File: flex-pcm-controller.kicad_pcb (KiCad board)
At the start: 2 copper layers, 36.6 x 35.6 mm, 19 parts, among them K1 POWER, K2 LOAD, Q1 PNP, Q2 MOSFET_DGS, Q3 MOSFET_GDS, U1 NE555N

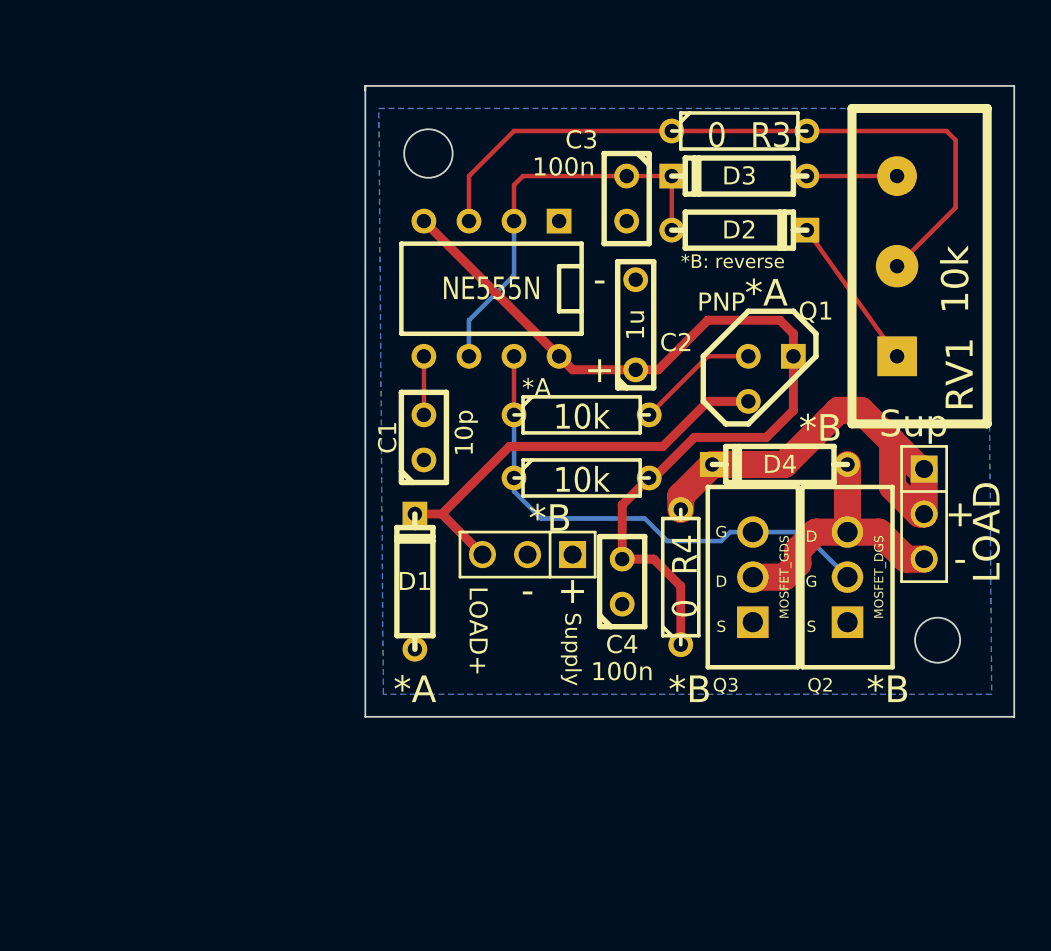
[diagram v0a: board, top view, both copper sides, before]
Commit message: Remove PNP option, lay out to take half of a 5cm^2 board
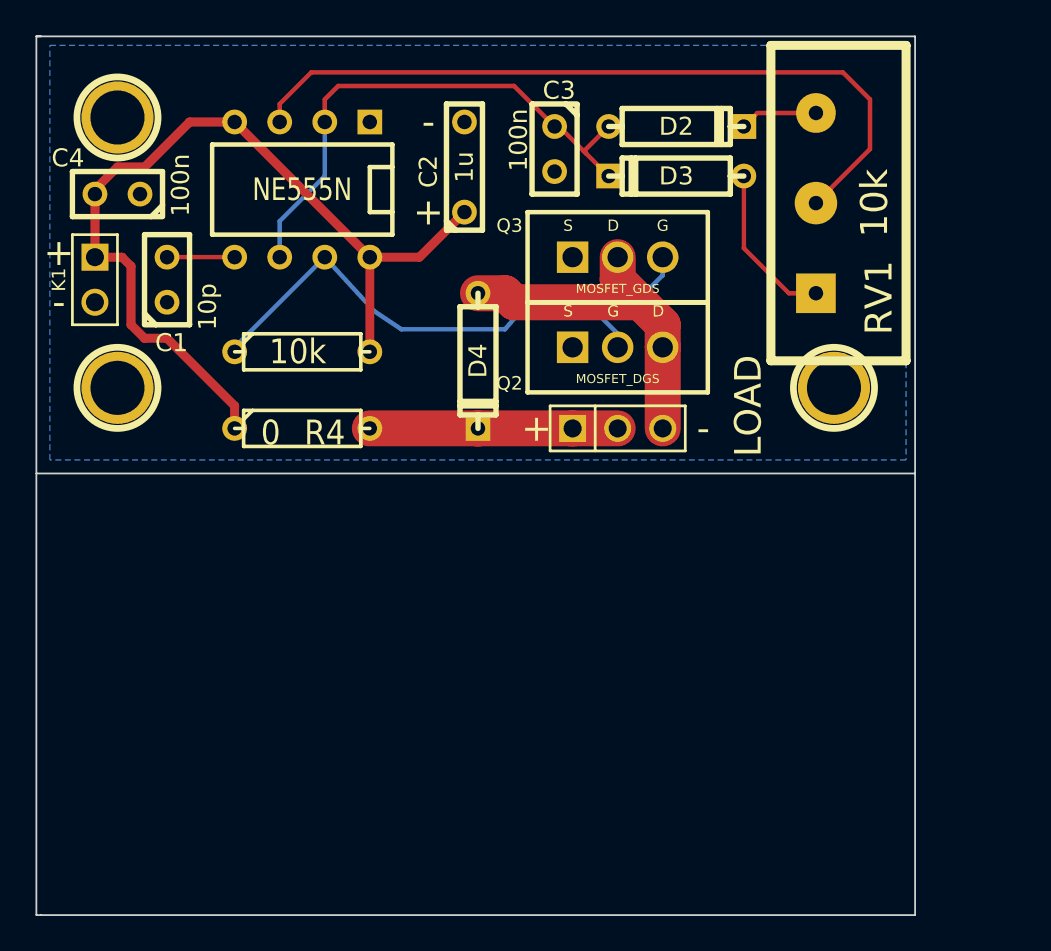
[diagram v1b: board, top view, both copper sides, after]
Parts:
- removed D1: DIODESCH, D3
- removed Q1: PNP, TO92
- removed R1: 10k, R3
- removed R3: 0, R3
- added 1PIN: P***, 1pin, F.Cu at (24.6, 24.6)
- added 1PIN: P***, 1pin, F.Cu at (65.0, 39.9)
- added 1PIN: P***, 1pin, F.Cu at (24.6, 39.9)
- K1: footprint PIN_ARRAY_3X1 -> PIN_ARRAY_2X1
- moved C4 35.9 mm to (24.6, 29.0), turned to 180 degrees
- moved K1 28.9 mm to (23.4, 33.8), turned to 270 degrees
- moved R4 22.9 mm to (35.1, 42.2), turned to 0 degrees
- moved Q3 19.6 mm to (52.8, 32.5), turned to 270 degrees
- moved Q2 18.3 mm to (52.8, 37.6), turned to 270 degrees
- moved D4 18.0 mm to (45.0, 38.4), turned to 270 degrees
- moved K2 17.9 mm to (52.8, 42.2), turned to 0 degrees
- moved R2 17.3 mm to (35.1, 37.8)
- moved C1 17.0 mm to (27.4, 33.8)
- moved C2 13.1 mm to (44.2, 27.4)
- moved U1 12.0 mm to (35.1, 28.7)
- moved D2 6.84 mm to (56.1, 25.1)
- moved RV1 5.79 mm to (69.1, 29.5)
- moved C3 4.93 mm to (49.3, 26.4)
- moved D3 3.56 mm to (56.1, 27.9)
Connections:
- D2 pad 2: N-0000011 -> N-000005
- D3 pad 1: N-0000010 (its old number) -> N-000007
- RV1 pad 1: N-0000011 -> N-000007
- RV1 pad 3: N-0000010 (its old number) -> N-000005
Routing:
- net /Vload: track 24.7 -> 0.00 mm
- net /Vload+: track 25.3 -> 14.0 mm
- net N-000007: track 0.00 -> 9.18 mm
- net N-0000011: track 8.74 -> 0.00 mm
- net N-0000010: track 22.9 -> 30.5 mm
- net N-0000012: track 6.96 -> 0.00 mm
- net /SIG: track 28.8 -> 34.1 mm
- net N-0000010 (its old number): track 5.08 -> 0.00 mm
- net /Vload-: track 15.6 -> 20.1 mm
- net N-000005: track 0.00 -> 4.38 mm
- net N-000006: track 39.7 -> 42.8 mm
- net VCC: track 52.2 -> 50.3 mm
- net N-000009: track 3.30 -> 3.81 mm
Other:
- board size 36.6 x 35.6 mm -> 49.5 x 49.5 mm
- net class HiPower: trace_width 1.524 -> 2.032
- board text removed: "*A"
- board text removed: "*B"
- board text removed: "*B: reverse"
- board text removed: "LOAD+"
- board text removed: "Sup"
- board text removed: "Supply"
